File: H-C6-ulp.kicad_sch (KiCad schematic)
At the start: 77 parts, among them J1 USB_C_Receptacle_USB2.0, J2 AFC24-S24FIC-00, J3 SM02B-SRSS-TB(LF)(SN), J4 SM04B-SRSS-TB_LF__SN_, Q1 Si1308, Q2 Si2301CDS, SW1 SW_Push_Dual, SW2 SW_Push_Dual, U1 ESP32-C6, U2 SGM6029CYG/TR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

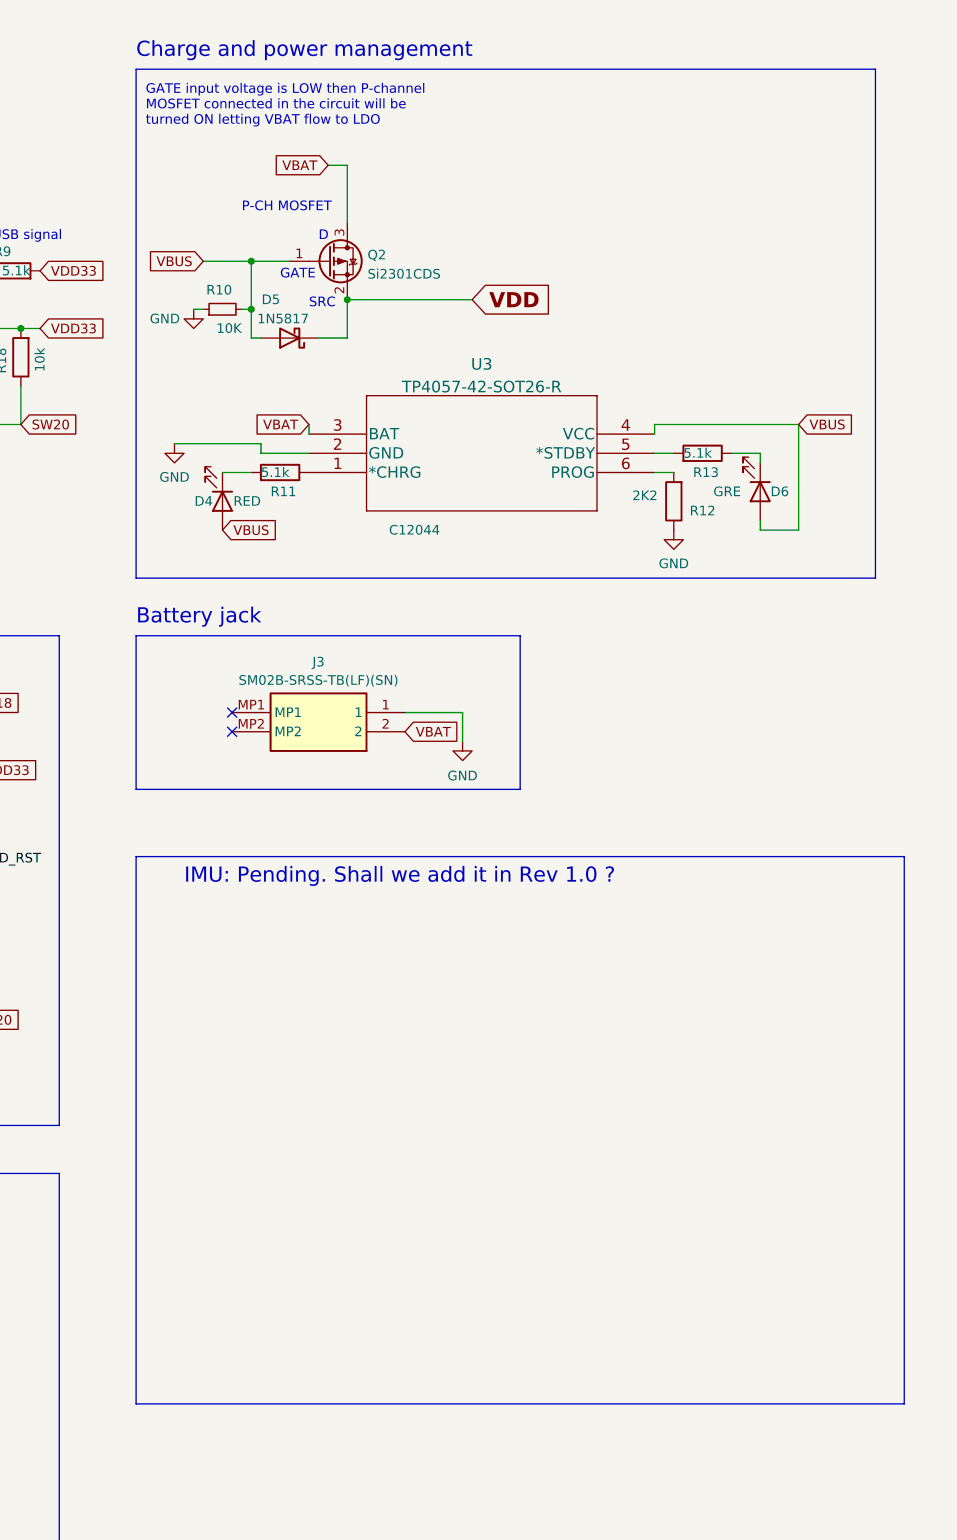
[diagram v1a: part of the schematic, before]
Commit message: Add 1mm TP for coin battery (Passes through regulator also)
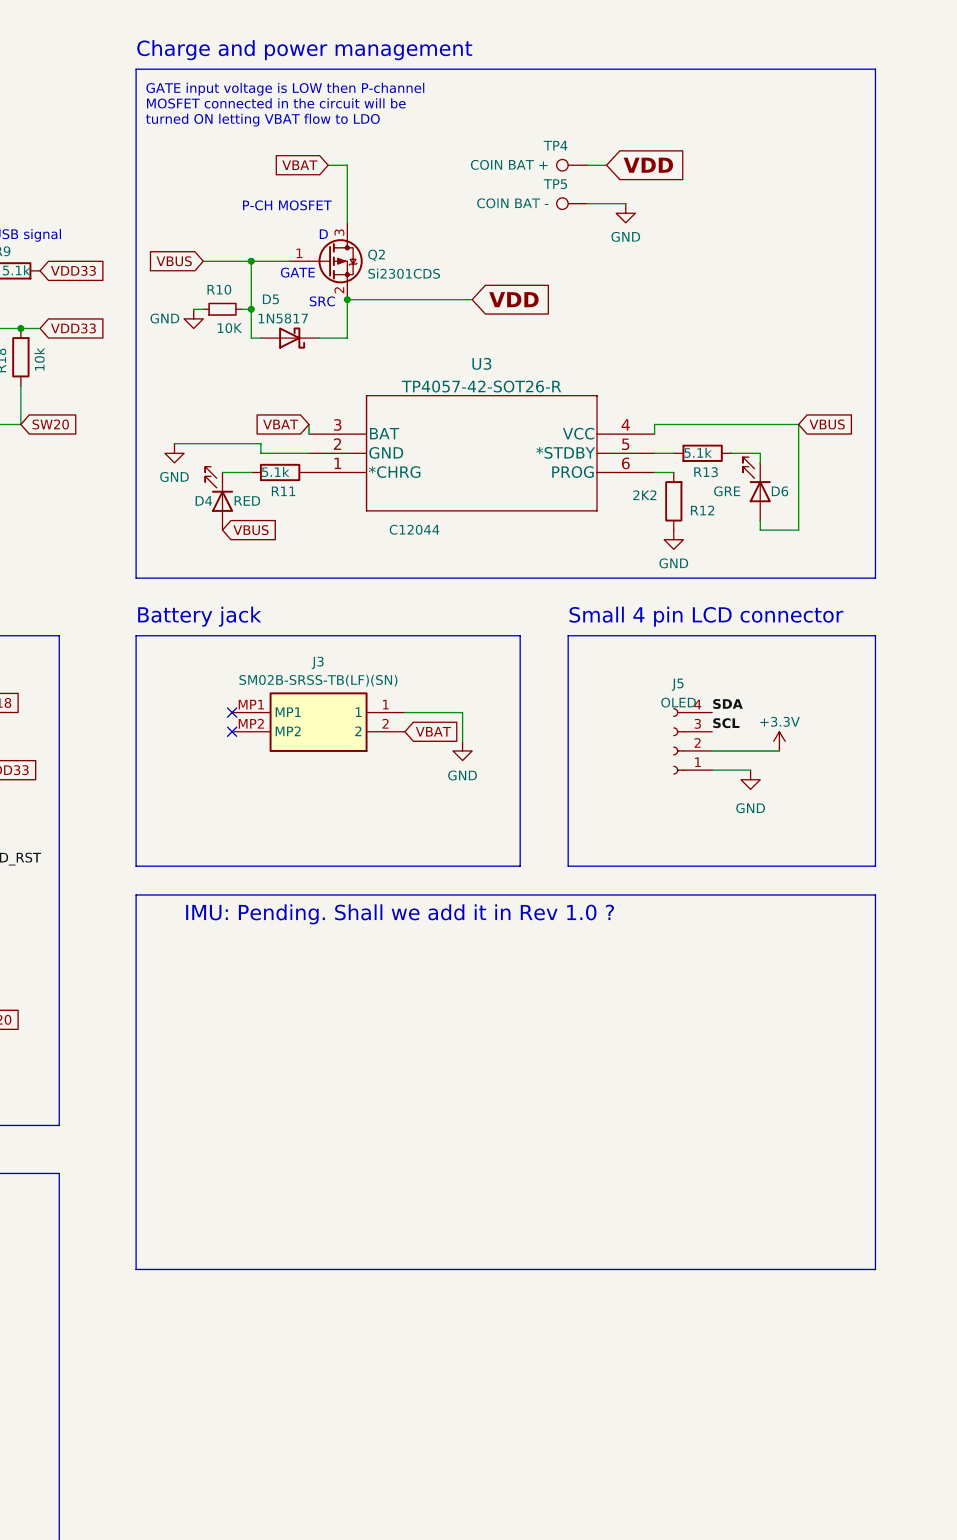
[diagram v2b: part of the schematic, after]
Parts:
- added J5: OLED, Connector_PinSocket_2.54mm:PinSocket_1x04_P2.54mm_Vertical, symbol Connector:Conn_01x04_Socket
- added TP4: COIN BAT +, TestPoint:TestPoint_Pad_D1.0mm, symbol Connector:TestPoint
- added TP5: COIN BAT -, TestPoint:TestPoint_Pad_D1.0mm, symbol Connector:TestPoint
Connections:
- net GND: now also J5.1 (Pin_1), TP5.1
- net SCL: now also J5.3 (Pin_3)
- net SDA: now also J5.4 (Pin_4)
- net VDD: now also TP4.1
- new net +3.3V: J5.2 (Pin_2)
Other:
- note added: "Small 4 pin LCD connector"
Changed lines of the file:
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@@
     (stroke (width 0) (type default))
   )
+  (wire (pts (xy 355.6 72.39) (xy 350.52 72.39))
+    (stroke (width 0) (type default))
+  )
   (wire (pts (xy 57.15 73.66) (xy 60.96 73.66))
     (stroke (width 0) (type default))
@@
     (stroke (width 0) (type default))
   )
-  (polyline (pts (xy 341.63 129.54) (xy 341.63 149.86))
+  (polyline (pts (xy 341.63 129.54) (xy 341.63 160.02))
     (stroke (width 0) (type default))
   )
@@
     (stroke (width 0) (type default))
   )
+  (wire (pts (xy 367.03 144.78) (xy 375.92 144.78))
+    (stroke (width 0) (type default))
+  )
   (wire (pts (xy 71.12 110.49) (xy 71.12 102.87))
     (stroke (width 0) (type default))
@@
     (stroke (width 0) (type default))
   )
+  (wire (pts (xy 353.06 67.31) (xy 350.52 67.31))
+    (stroke (width 0) (type default))
+  )
   (wire (pts (xy 90.17 246.38) (xy 90.17 243.84))
     (stroke (width 0) (type default))
@@
     (stroke (width 0) (type default))
   )
-  (polyline (pts (xy 290.83 129.54) (xy 290.83 149.86))
+  (polyline (pts (xy 290.83 129.54) (xy 290.83 160.02))
     (stroke (width 0) (type default))
   )
@@
     (stroke (width 0) (type default))
   )
-  (polyline (pts (xy 341.63 149.86) (xy 290.83 149.86))
+  (polyline (pts (xy 341.63 160.02) (xy 290.83 160.02))
     (stroke (width 0) (type default))
   )
@@
     (stroke (width 0) (type default))
   )
+  (wire (pts (xy 367.03 147.32) (xy 372.11 147.32))
+    (stroke (width 0) (type default))
+  )
   (polyline (pts (xy 115.57 194.31) (xy 180.34 194.31))
     (stroke (width 0) (type default))
@@
     (stroke (width 0) (type default))
   )
+  (rectangle (start 347.98 129.54) (end 388.62 160.02)
+    (stroke (width 0) (type default))
+    (fill (type none))
+  )
   (rectangle (start 20.32 200.66) (end 73.66 273.05)
     (stroke (width 0) (type default))
@@
     (fill (type none))
   )
-  (rectangle (start 290.83 158.75) (end 392.43 231.14)
+  (rectangle (start 290.83 163.83) (end 388.62 213.36)
     (stroke (width 0) (type default))
     (fill (type none))
@@
     (effects (font (size 1.27 1.27)) (justify left bottom))
   )
-  (text "IMU: Pending. Shall we add it in Rev 1.0 ?" (at 297.18 162.56 0)
+  (text "IMU: Pending. Shall we add it in Rev 1.0 ?" (at 297.18 167.64 0)
     (effects (font (size 2 2)) (justify left bottom))
   )
@@
     (effects (font (size 1.27 1.27)) (justify left bottom))
   )
+  (text "Small 4 pin LCD connector" (at 347.98 128.27 0)
+    (effects (font (size 2 2)) (justify left bottom))
+  )
   (text "VSH" (at 36.83 132.08 0)
     (effects (font (size 1.27 1.27)) (justify left bottom))
@@
     (effects (font (size 1.27 1.27)) (justify left bottom))
   )
+  (label "SDA" (at 367.03 139.7 0) (fields_autoplaced)
+    (effects (font (size 1.27 1.27) (thickness 0.254) bold (color 0 194 0 1)) (justify left bottom))
+  )
   (label "EPD_CS" (at 36.83 111.76 0) (fields_autoplaced)
     (effects (font (size 1.27 1.27)) (justify left bottom))
@@
     (effects (font (size 1.27 1.27) (color 194 0 194 1)) (justify left bottom))
   )
+  (label "SCL" (at 367.03 142.24 0) (fields_autoplaced)
+    (effects (font (size 1.27 1.27) (thickness 0.254) bold (color 0 194 0 1)) (justify left bottom))
+  )
   (label "EPD_CLK" (at 186.69 68.58 180) (fields_autoplaced)
     (effects (font (size 1.27 1.27)) (justify right bottom))
@@
     )
   )
+  (global_label "VDD" (shape input) (at 353.06 67.31 0) (fields_autoplaced)
+    (effects (font (size 2 2) (thickness 0.4) bold (color 194 0 0 1)) (justify left))
+    (property "Intersheetrefs" "${INTERSHEET_REFS}" (at 364.2246 67.31 0)
+      (effects (font (size 1.27 1.27)) (justify left) hide)
+    )
+  )
   (global_label "VBAT" (shape input) (at 316.23 67.31 180) (fields_autoplaced)
     (effects (font (size 1.27 1.27)) (justify right))
@@
     )
   )
+  (symbol (lib_id "power:+3.3V") (at 375.92 144.78 0) (unit 1)
+    (in_bom yes) (on_board yes) (dnp no) (fields_autoplaced)
+    (property "Reference" "#PWR048" (at 375.92 148.59 0)
+      (effects (font (size 1.27 1.27)) hide)
+    )
+    (property "Value" "+3.3V" (at 375.92 140.97 0)
+      (effects (font (size 1.27 1.27)))
+    )
+    (property "Footprint" "" (at 375.92 144.78 0)
+      (effects (font (size 1.27 1.27)) hide)
+    )
+    (property "Datasheet" "" (at 375.92 144.78 0)
+      (effects (font (size 1.27 1.27)) hide)
+    )
+    (pin "1")
+    (instances
+      (project "H-C6-ulp"
+        (path "/4820ae53-5724-49d2-a676-459cc31081bd"
+          (reference "#PWR048") (unit 1)
+        )
+      )
+    )
+  )
   (symbol (lib_id "QWIIC:SM04B-SRSS-TB_LF__SN_") (at 31.75 231.14 0) (unit 1)
     (in_bom yes) (on_board yes) (dnp no)
@@
     )
   )
+  (symbol (lib_id "power:GND") (at 372.11 147.32 0) (unit 1)
+    (in_bom yes) (on_board yes) (dnp no) (fields_autoplaced)
+    (property "Reference" "#PWR047" (at 372.11 153.67 0)
+      (effects (font (size 1.27 1.27)) hide)
+    )
+    (property "Value" "GND" (at 372.11 152.4 0)
+      (effects (font (size 1.27 1.27)))
+    )
+    (property "Footprint" "" (at 372.11 147.32 0)
+      (effects (font (size 1.27 1.27)) hide)
+    )
+    (property "Datasheet" "" (at 372.11 147.32 0)
+      (effects (font (size 1.27 1.27)) hide)
+    )
+    (pin "1")
+    (instances
+      (project "H-C6-ulp"
+        (path "/4820ae53-5724-49d2-a676-459cc31081bd"
+          (reference "#PWR047") (unit 1)
+        )
+      )
+    )
+  )
   (symbol (lib_id "Device:C") (at 68.58 135.89 270) (unit 1)
     (in_bom yes) (on_board yes) (dnp no)
@@
     )
   )
+  (symbol (lib_id "Connector:TestPoint") (at 350.52 67.31 90) (unit 1)
+    (in_bom yes) (on_board yes) (dnp no)
+    (property "Reference" "TP4" (at 347.98 64.77 90)
+      (effects (font (size 1.27 1.27)) (justify left))
+    )
+    (property "Value" "COIN BAT +" (at 345.44 67.31 90)
+      (effects (font (size 1.27 1.27)) (justify left))
+    )
+    (property "Footprint" "TestPoint:TestPoint_Pad_D1.0mm" (at 350.52 62.23 0)
+      (effects (font (size 1.27 1.27)) hide)
+    )
+    (property "Datasheet" "~" (at 350.52 62.23 0)
+      (effects (font (size 1.27 1.27)) hide)
+    )
+    (pin "1")
+    (instances
+      (project "H-C6-ulp"
+        (path "/4820ae53-5724-49d2-a676-459cc31081bd"
+          (reference "TP4") (unit 1)
+        )
+      )
+    )
+  )
   (symbol (lib_id "Mechanical:MountingHole") (at 54.61 185.42 0) (unit 1)
     (in_bom no) (on_board yes) (dnp no)
@@
     )
   )
+  (symbol (lib_id "Connector:TestPoint") (at 350.52 72.39 90) (unit 1)
+    (in_bom yes) (on_board yes) (dnp no)
+    (property "Reference" "TP5" (at 347.98 69.85 90)
+      (effects (font (size 1.27 1.27)) (justify left))
+    )
+    (property "Value" "COIN BAT -" (at 345.44 72.39 90)
+      (effects (font (size 1.27 1.27)) (justify left))
+    )
+    (property "Footprint" "TestPoint:TestPoint_Pad_D1.0mm" (at 350.52 67.31 0)
+      (effects (font (size 1.27 1.27)) hide)
+    )
+    (property "Datasheet" "~" (at 350.52 67.31 0)
+      (effects (font (size 1.27 1.27)) hide)
+    )
+    (pin "1")
+    (instances
+      (project "H-C6-ulp"
+        (path "/4820ae53-5724-49d2-a676-459cc31081bd"
+          (reference "TP5") (unit 1)
+        )
+      )
+    )
+  )
   (symbol (lib_id "TP4057:TP4057-42-SOT26-R") (at 313.69 107.95 0) (mirror x) (unit 1)
     (in_bom yes) (on_board yes) (dnp no)
@@
     )
   )
+  (symbol (lib_id "power:GND") (at 355.6 72.39 0) (unit 1)
+    (in_bom yes) (on_board yes) (dnp no) (fields_autoplaced)
+    (property "Reference" "#PWR049" (at 355.6 78.74 0)
+      (effects (font (size 1.27 1.27)) hide)
+    )
+    (property "Value" "GND" (at 355.6 76.8334 0)
+      (effects (font (size 1.27 1.27)))
+    )
+    (property "Footprint" "" (at 355.6 72.39 0)
+      (effects (font (size 1.27 1.27)) hide)
+    )
+    (property "Datasheet" "" (at 355.6 72.39 0)
+      (effects (font (size 1.27 1.27)) hide)
+    )
+    (pin "1")
+    (instances
+      (project "H-C6-ulp"
+        (path "/4820ae53-5724-49d2-a676-459cc31081bd"
+          (reference "#PWR049") (unit 1)
+        )
+      )
+    )
+  )
   (symbol (lib_id "power:PWR_FLAG") (at 214.63 233.68 0) (unit 1)
     (in_bom yes) (on_board yes) (dnp no)
@@
         )
       )
+    )
+  )
+  (symbol (lib_id "Connector:Conn_01x04_Socket") (at 361.95 144.78 180) (unit 1)
+    (in_bom yes) (on_board yes) (dnp no) (fields_autoplaced)
+    (property "Reference" "J5" (at 362.585 135.89 0)
+      (effects (font (size 1.27 1.27)))
+    )
+    (property "Value" "OLED" (at 362.585 138.43 0)
+      (effects (font (size 1.27 1.27)))
+    )
+    (property "Footprint" "Connector_PinSocket_2.54mm:PinSocket_1x04_P2.54mm_Vertical" (at 361.95 144.78 0)
+      (effects (font (size 1.27 1.27)) hide)
+    )
+    (property "Datasheet" "~" (at 361.95 144.78 0)
+      (effects (font (size 1.27 1.27)) hide)
+    )
+    (pin "1")
+    (pin "2")
+    (pin "3")
+    (pin "4")
+    (instances
+      (project "H-C6-ulp"
+        (path "/4820ae53-5724-49d2-a676-459cc31081bd"
+          (reference "J5") (unit 1)
+        )
+      )
